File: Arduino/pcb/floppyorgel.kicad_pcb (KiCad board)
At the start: 2 copper layers, 50 x 50 mm, 48 parts, among them J1 VCC_Power_Select, J2 Floppy-Bus, J3 MAX485 Socket, J4 Floppy-Bus, J5 Buck-Converter-5V, J6 Buck-Converter-12V, J7 Floppy-Power, J8 IBM_PC_Floppy_IDC, J9 FTDI, Q1 IRLML2060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

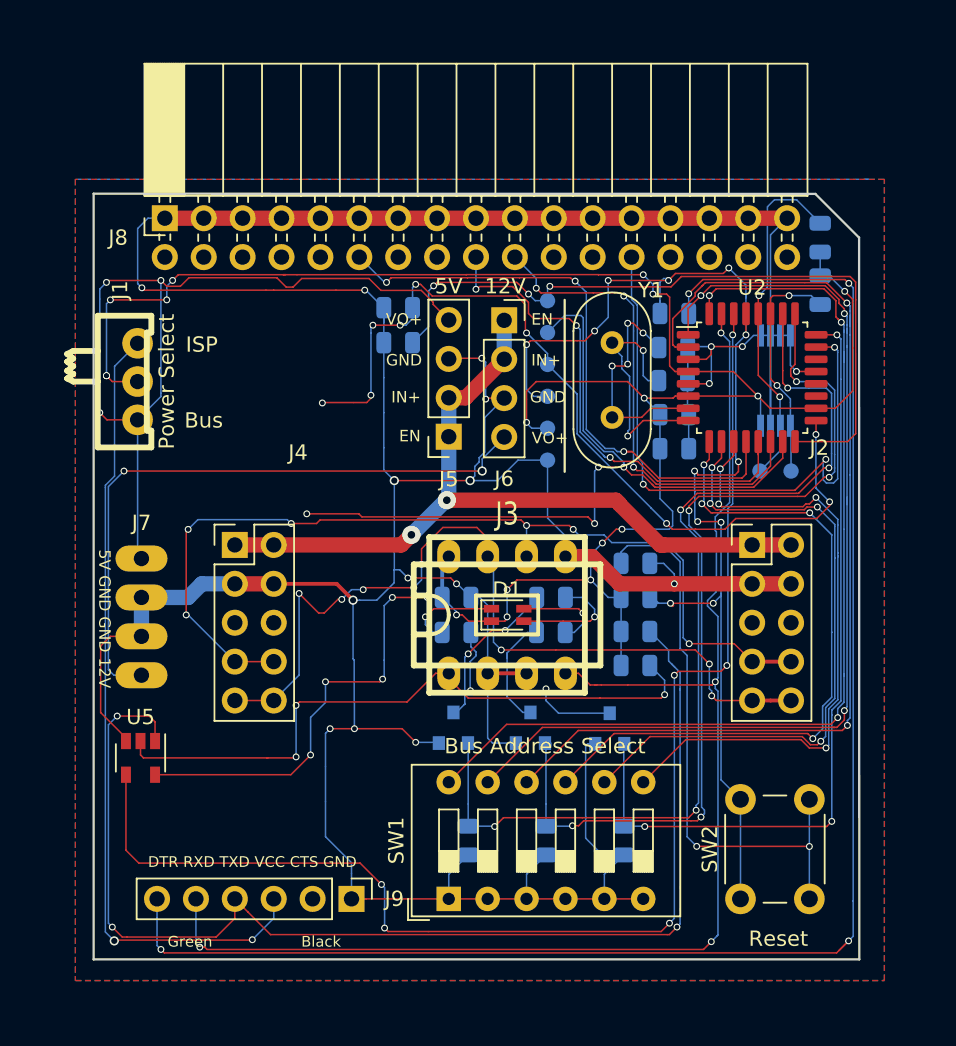
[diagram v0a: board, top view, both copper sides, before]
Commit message: pcb: route RS485 control pins
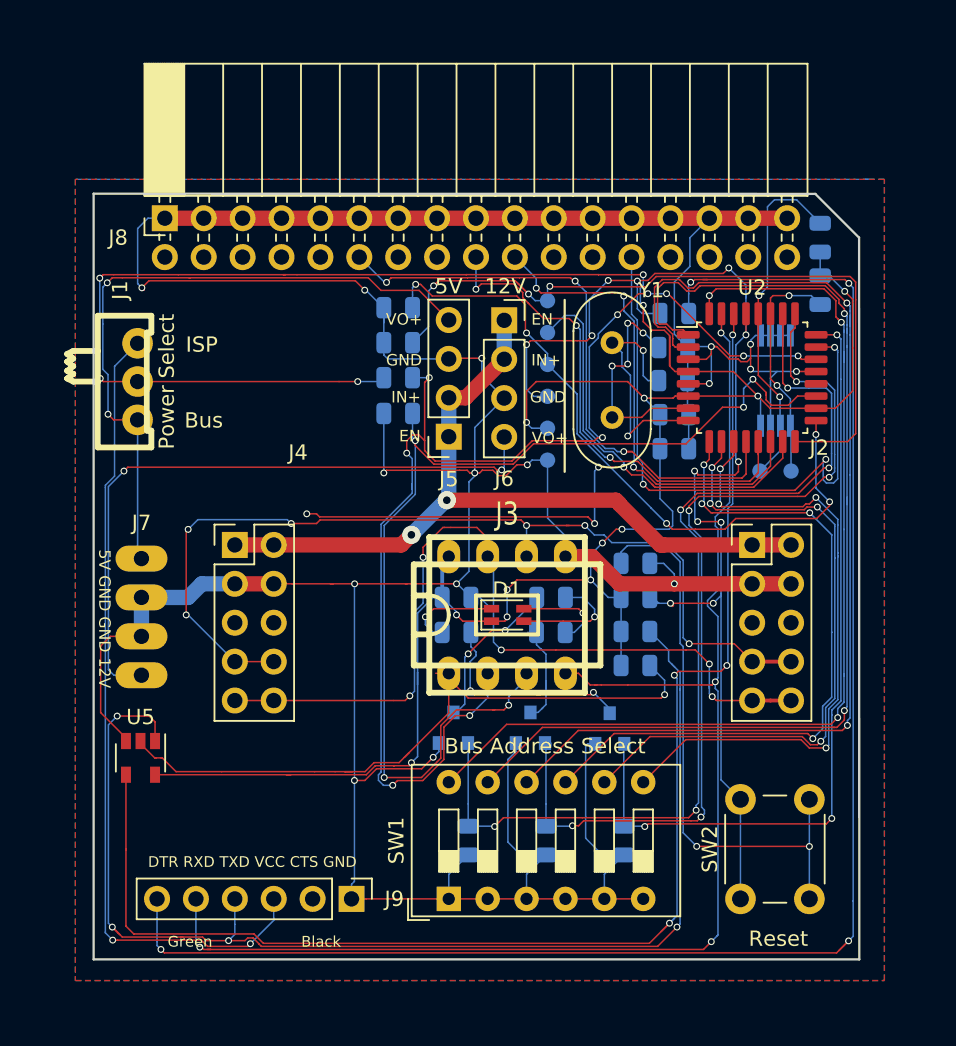
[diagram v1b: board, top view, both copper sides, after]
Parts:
- added R1: 4k7, Resistor_SMD:R_0805_2012Metric, B.Cu at (119.9, 112.0)
- added R2: 4k7, Resistor_SMD:R_0805_2012Metric, B.Cu at (119.9, 114.4)
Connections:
- J3 pad 2: GND -> /Bus/BUS_RX_EN
- J3 pad 3: GND -> /Bus/BUS_TX_EN
- U2 pad 19: (no net) -> /Bus/BUS_TX_EN
- U2 pad 22: (no net) -> /Bus/BUS_RX_EN
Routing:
- net /Bus/BUS_RX_EN: track 0.00 -> 82.2 mm, vias 0 -> 10
- net /Bus/BUS_TX_EN: track 0.00 -> 70.2 mm, vias 0 -> 5
- net VCC: track 164.8 -> 186.1 mm, vias 22 -> 16
- net /MCU/SCK: track 56.5 -> 44.9 mm, vias 9 -> 5
- net /5V_BUS: track 55.1 -> 43.7 mm, vias 3 -> 2
- net GND: track 290.7 -> 284.3 mm, vias 17 -> 16
- net /Floppy/A2: track 66.2 -> 70.9 mm, vias 3 -> 2
- net Net-(U2-Pad30): track 87.5 -> 90.9 mm, vias 6 -> 4
- net /Floppy/A3: track 66.8 -> 70.2 mm
- net Net-(J9-Pad4): track 78.9 -> 80.6 mm, vias 3 -> 4
- net /Bus/BUS_TX: track 42.8 -> 44.4 mm, vias 3 -> 1
- net /MCU/MISO: track 48.1 -> 49.6 mm
- net /Floppy/12V_BUS: track 42.8 -> 43.6 mm
- net Net-(C3-Pad2): track 105.0 -> 105.7 mm
- net /5V_ISP: track 52.4 -> 52.9 mm
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
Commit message: pcb: do some final optimizations for v3.1
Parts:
- added J10: AVR-ISP, Connector_PinHeader_2.54mm:PinHeader_2x03_P2.54mm_Vertical, F.Cu at (110.8, 113.5)
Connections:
- TP5 pad 1: VCC -> /5V_ISP
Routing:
- net /5V_ISP: track 52.9 -> 91.0 mm, vias 2 -> 4
- net /MCU/MISO: track 49.6 -> 68.4 mm, vias 3 -> 6
- net /MCU/SCK: track 44.9 -> 61.1 mm, vias 5 -> 7
- net /MCU/RESET: track 79.9 -> 94.5 mm, vias 12 -> 13
- net VCC: track 186.1 -> 174.2 mm, vias 16 -> 15
- net Net-(R10-Pad1): track 38.1 -> 49.5 mm, vias 2 -> 3
- net /MCU/MOSI: track 51.5 -> 60.6 mm
- net /Bus/BP: track 61.8 -> 54.8 mm, vias 6 -> 4
- net GND: track 284.3 -> 279.6 mm, vias 16 -> 17
- net /Bus/BUS_RX_EN: track 82.2 -> 78.8 mm, vias 10 -> 9
- net /Floppy/12V_BUS: track 43.6 -> 44.6 mm
- net /Bus/BUS_TX_EN: track 70.2 -> 70.9 mm
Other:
- board text added: "coon 16.10.2019"
- board text removed: "coon 17.07.2019"

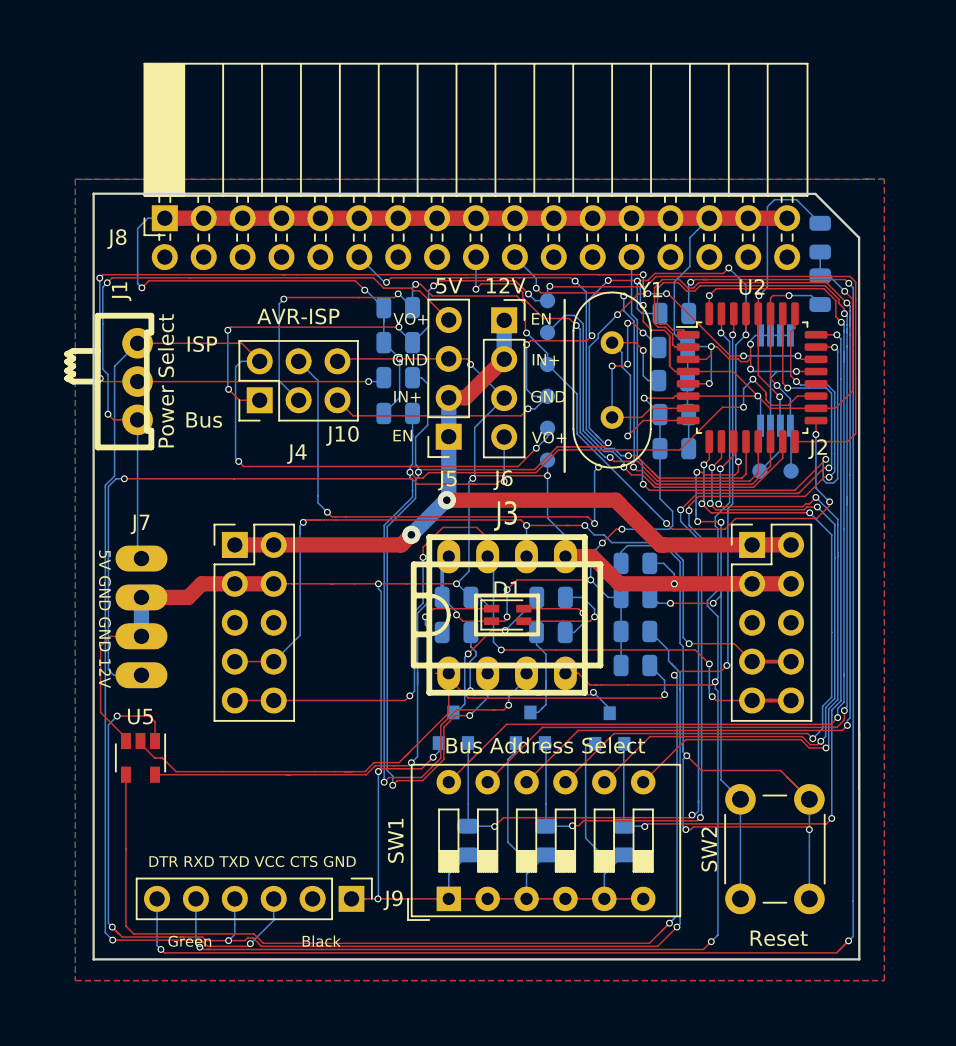
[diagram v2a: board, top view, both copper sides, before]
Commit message: pcb: increase board dimensions by 5x5mm + delete all tracks
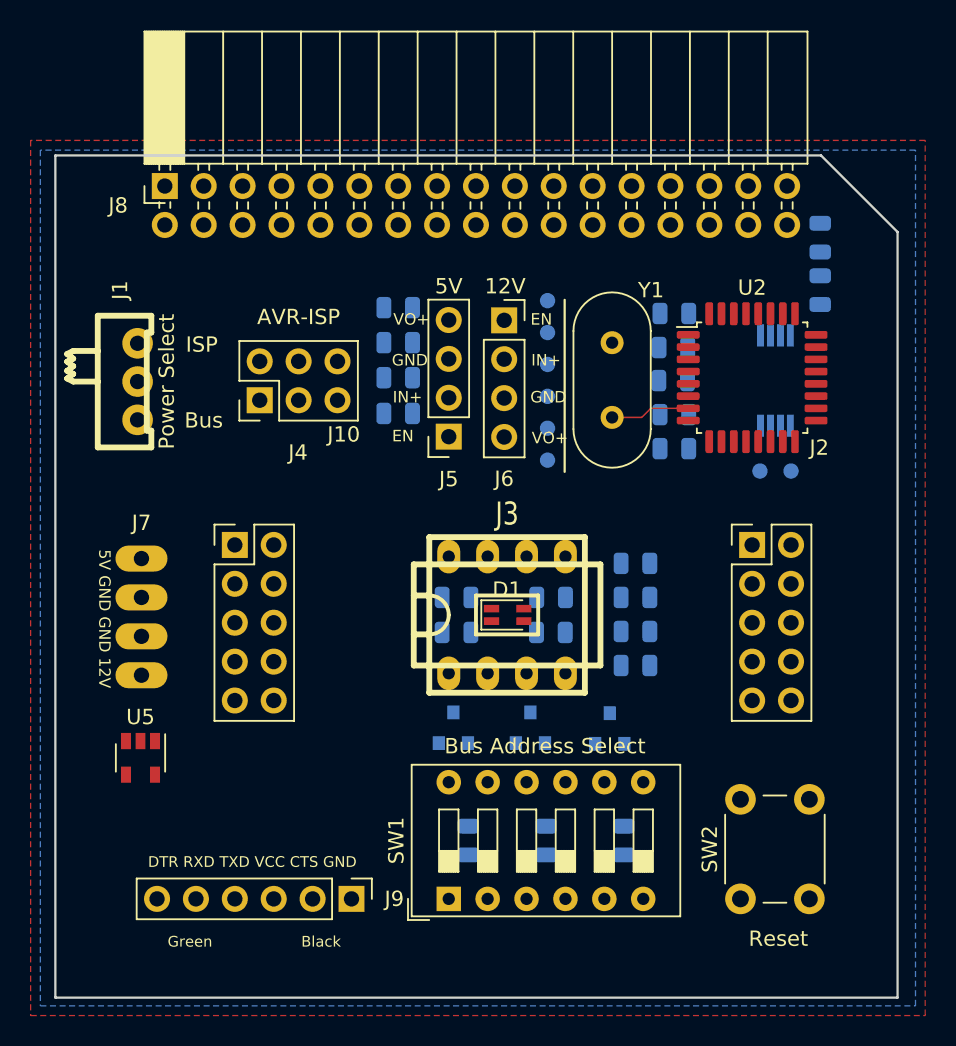
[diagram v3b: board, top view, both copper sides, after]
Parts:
- moved J8 2.10 mm to (104.6, 99.5)
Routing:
- net GND: track 279.6 -> 0.00 mm, vias 17 -> 0
- net VCC: track 174.2 -> 0.00 mm, vias 15 -> 0
- net Net-(C3-Pad2): track 105.7 -> 0.00 mm, vias 4 -> 0
- net /MCU/RESET: track 94.5 -> 0.00 mm, vias 13 -> 0
- net /5V_ISP: track 91.0 -> 0.00 mm, vias 4 -> 0
- net Net-(U2-Pad30): track 90.9 -> 0.00 mm, vias 4 -> 0
- net /Bus/BUS_RX: track 90.1 -> 0.00 mm, vias 4 -> 0
- net Net-(J9-Pad4): track 80.6 -> 0.00 mm, vias 4 -> 0
- net /Bus/BUS_RX_EN: track 78.8 -> 0.00 mm, vias 9 -> 0
- net /Floppy/A2: track 70.9 -> 0.00 mm, vias 2 -> 0
- net /Bus/BUS_TX_EN: track 70.9 -> 0.00 mm, vias 5 -> 0
- net /Floppy/A3: track 70.2 -> 0.00 mm, vias 2 -> 0
- net /MCU/MISO: track 68.4 -> 0.00 mm, vias 6 -> 0
- net /Floppy/A1: track 65.4 -> 0.00 mm, vias 3 -> 0
- net /Led/LED_BLUE: track 64.9 -> 0.00 mm, vias 5 -> 0
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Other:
- board size 50 x 50 mm -> 55 x 55 mm
- board text added: "Floppy Module 3.2"
- board text removed: "Floppy Module 3.1"

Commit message: pcb: begin routing for v3.2
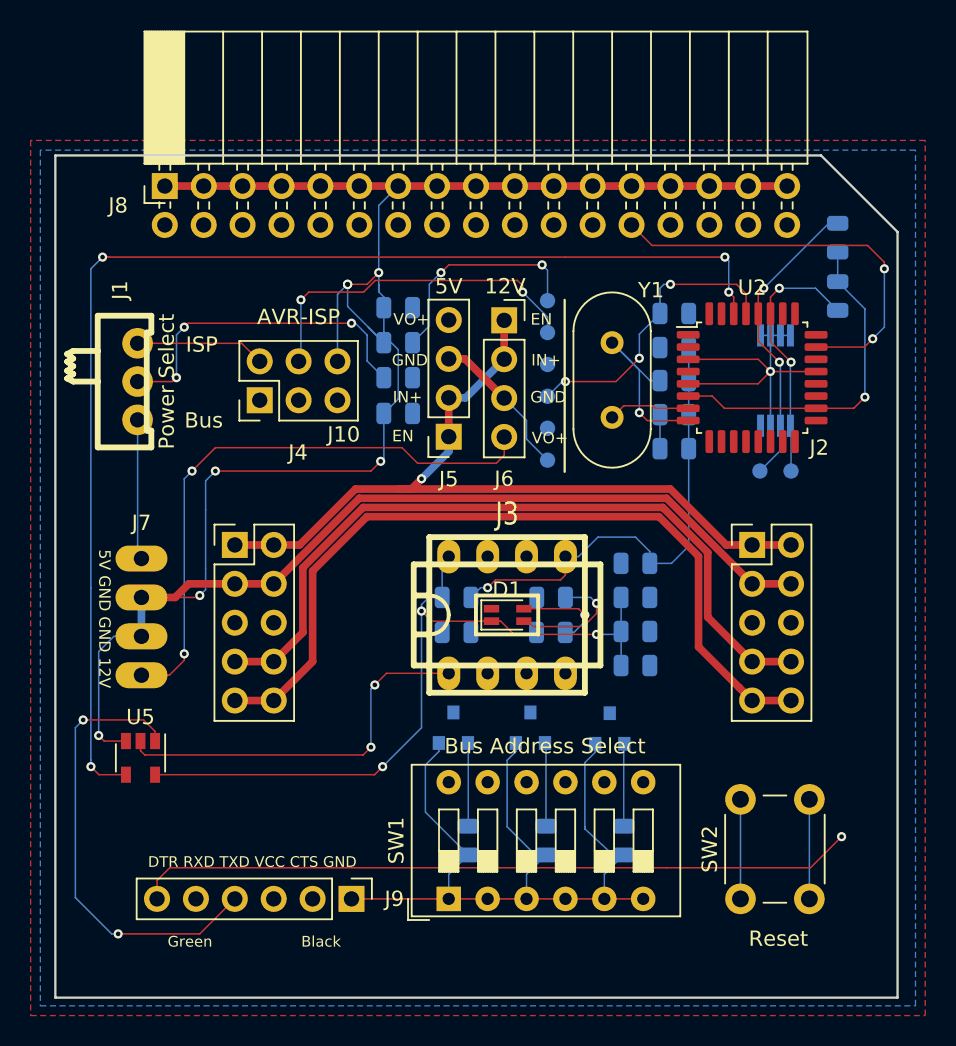
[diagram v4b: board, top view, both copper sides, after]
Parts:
- moved R20 1.20 mm to (148.6, 106.7)
- moved R21 1.14 mm to (148.6, 102.9)
- moved C5 0.08 mm to (137.9, 112.2)
- moved C4 0.06 mm to (137.9, 110.0)
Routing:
- net GND: track 0.00 -> 279.0 mm, vias 0 -> 9
- net VCC: track 0.00 -> 95.7 mm, vias 0 -> 7
- net Net-(U2-Pad30): track 0.00 -> 80.7 mm, vias 0 -> 4
- net /Bus/BUS_POWER: track 0.00 -> 54.3 mm, vias 0 -> 1
- net /Bus/BM: track 0.00 -> 53.2 mm
- net /Bus/BP: track 0.00 -> 49.6 mm
- net Net-(C3-Pad2): track 0.00 -> 47.1 mm, vias 0 -> 1
- net /Floppy/12V_BUS: track 0.00 -> 38.6 mm, vias 0 -> 2
- net Net-(J9-Pad4): track 0.00 -> 29.8 mm, vias 0 -> 2
- net /Floppy/TRK00: track 0.00 -> 26.8 mm, vias 0 -> 2
- net /MCU/RESET: track 0.00 -> 25.9 mm, vias 0 -> 3
- net /Bus/BUS_TX: track 0.00 -> 25.3 mm, vias 0 -> 2
- net /MCU/MOSI: track 0.00 -> 23.0 mm, vias 0 -> 2
- net /MCU/SCL: track 0.00 -> 19.8 mm, vias 0 -> 2
- net /MCU/SDA: track 0.00 -> 17.2 mm, vias 0 -> 2
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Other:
- net class Default: via_dia 0.45 -> 0.6
- rule via_min_drill: 0.2 -> 0.3

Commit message: pcb: rename RS485 bus pins + differential pair routing
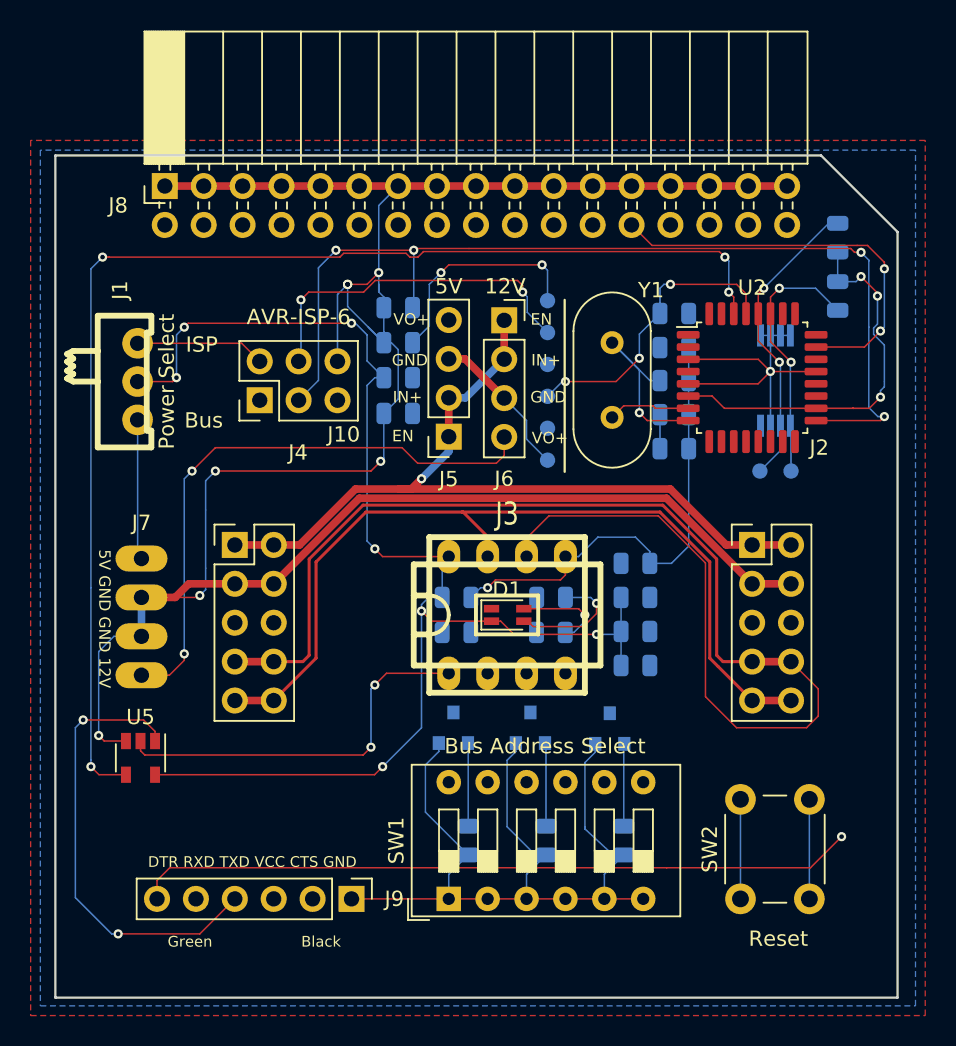
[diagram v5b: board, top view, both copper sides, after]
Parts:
- J10: value AVR-ISP -> AVR-ISP-6
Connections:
- net /Bus/BM renamed /Bus/BUS-
- net /Bus/BP renamed /Bus/BUS+
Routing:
- net /MCU/SCK: track 0.00 -> 65.2 mm, vias 0 -> 4
- net /Bus/BUS+: track 49.6 -> 88.5 mm
- net VCC: track 95.7 -> 116.2 mm, vias 7 -> 10
- net /Bus/BUS-: track 53.2 -> 57.5 mm
- net Net-(U2-Pad30): track 80.7 -> 81.2 mm
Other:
- net class Differential added: clearance 0.1, trace_width 0.5, via_dia 0.6, via_drill 0.3
- board text added: "BUS+"
- board text added: "BUS-"
- board text removed: "BM"
- board text removed: "BP"

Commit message: pcb: more routing...
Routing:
- net /Floppy/A1: track 0.00 -> 85.0 mm, vias 0 -> 2
- net /Floppy/A2: track 0.00 -> 79.9 mm, vias 0 -> 2
- net /Floppy/A3: track 0.00 -> 76.3 mm, vias 0 -> 2
- net /Floppy/A5: track 0.00 -> 60.5 mm, vias 0 -> 2
- net /Floppy/A6: track 0.00 -> 58.1 mm, vias 0 -> 2
- net /Floppy/A4: track 0.00 -> 55.1 mm, vias 0 -> 2
- net Net-(C3-Pad2): track 47.1 -> 89.0 mm, vias 1 -> 3
- net /Bus/BUS+: track 88.5 -> 52.1 mm, vias 0 -> 3
- net GND: track 279.0 -> 311.9 mm, vias 9 -> 15
- net /5V_BUS: track 9.16 -> 39.4 mm, vias 0 -> 1
- net VCC: track 116.2 -> 132.1 mm, vias 10 -> 13
- net Net-(Q1-Pad3): track 0.00 -> 13.4 mm, vias 0 -> 2
- net Net-(Q3-Pad3): track 0.00 -> 11.6 mm
- net /MCU/SCK: track 65.2 -> 76.0 mm, vias 4 -> 5
- net /MCU/MOSI: track 23.0 -> 30.4 mm
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
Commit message: pcb: continue routing
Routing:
- net /5V_ISP: track 8.46 -> 80.4 mm, vias 0 -> 3
- net /Led/LED_BLUE: track 5.43 -> 69.7 mm, vias 0 -> 3
- net /Led/LED_GREEN: track 5.46 -> 59.4 mm, vias 0 -> 3
- net Net-(J9-Pad4): track 29.8 -> 78.1 mm, vias 2 -> 3
- net /Led/LED_RED: track 5.39 -> 51.5 mm, vias 0 -> 3
- net /Bus/BUS_RX: track 0.00 -> 37.9 mm, vias 0 -> 2
- net /Floppy/DRIVE_SELECT: track 0.00 -> 30.1 mm, vias 0 -> 1
- net /MCU/SCK: track 76.0 -> 101.9 mm, vias 5 -> 9
- net /MCU/MISO: track 14.6 -> 38.5 mm, vias 2 -> 4
- net VCC: track 132.1 -> 155.5 mm, vias 13 -> 17
- net /Bus/BUS+: track 52.1 -> 68.0 mm
- net Net-(C3-Pad2): track 89.0 -> 98.7 mm
- net /Bus/BUS-: track 53.8 -> 57.9 mm
- net /Floppy/A3: track 76.3 -> 78.3 mm, vias 2 -> 0
- net /Floppy/A1: track 85.0 -> 86.9 mm, vias 2 -> 0
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
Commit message: pcb: finish routing of v3.2
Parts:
- moved C5 2.32 mm to (137.9, 109.9)
- moved C4 2.12 mm to (137.9, 112.2)
- moved L1 1.35 mm to (108.9, 138.9)
- moved C3 0.23 mm to (137.9, 107.6)
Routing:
- net /Bus/BUS_RX_EN: track 0.00 -> 87.3 mm, vias 0 -> 9
- net /Bus/BUS_TX_EN: track 0.00 -> 86.4 mm, vias 0 -> 4
- net /Bus/BUS_RX: track 37.9 -> 113.9 mm, vias 2 -> 8
- net /MCU/RESET: track 29.2 -> 86.1 mm, vias 3 -> 8
- net /Floppy/DIRECTION: track 0.00 -> 48.2 mm, vias 0 -> 3
- net /Floppy/STEP: track 0.00 -> 47.0 mm, vias 0 -> 5
- net /MCU/MISO: track 38.5 -> 76.0 mm, vias 4 -> 7
- net /MCU/MOSI: track 30.4 -> 65.8 mm, vias 2 -> 4
- net Net-(R10-Pad1): track 6.50 -> 33.4 mm, vias 0 -> 3
- net /5V_ISP: track 80.4 -> 105.8 mm, vias 3 -> 7
- net /Bus/BUS_TX: track 25.3 -> 44.0 mm, vias 2 -> 3
- net /Floppy/DRIVE_SELECT: track 30.1 -> 41.0 mm, vias 1 -> 3
- net Net-(C3-Pad2): track 98.7 -> 89.7 mm
- net VCC: track 155.5 -> 161.5 mm, vias 17 -> 19
- net GND: track 312.2 -> 317.3 mm, vias 15 -> 16
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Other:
- board text added: "coon 21.02.2020"
- board text removed: "coon 16.10.2019"
